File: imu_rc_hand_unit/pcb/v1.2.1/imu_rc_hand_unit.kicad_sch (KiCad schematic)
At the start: 76 parts, among them J1 USB_C_Receptacle_USB2.0_16P, J2 JST SH1.0, Q1 IRLML6344TRPBF, Q2 IRLML6344TRPBF, Q3 DMP3160L-7, Q4 IRLML6344TRPBF, Q5 DMP3160L-7, Q6 BSS138, Q7 BC817-25, Q8 BC817-25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

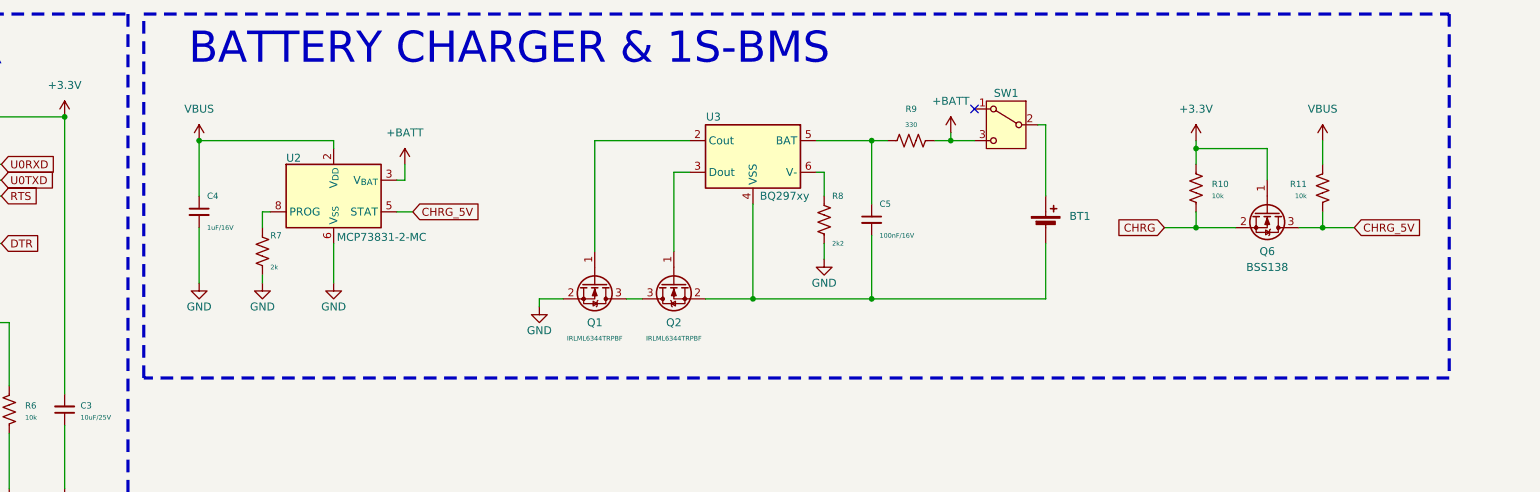
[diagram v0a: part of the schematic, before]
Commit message: commit #39
imu rc hand unit v1.2.2:
removed bq297
added ON/OFF text for switch

enclosure hand unit:
small hole changes inside (m3) and outside (m3)
led diameter hole increased
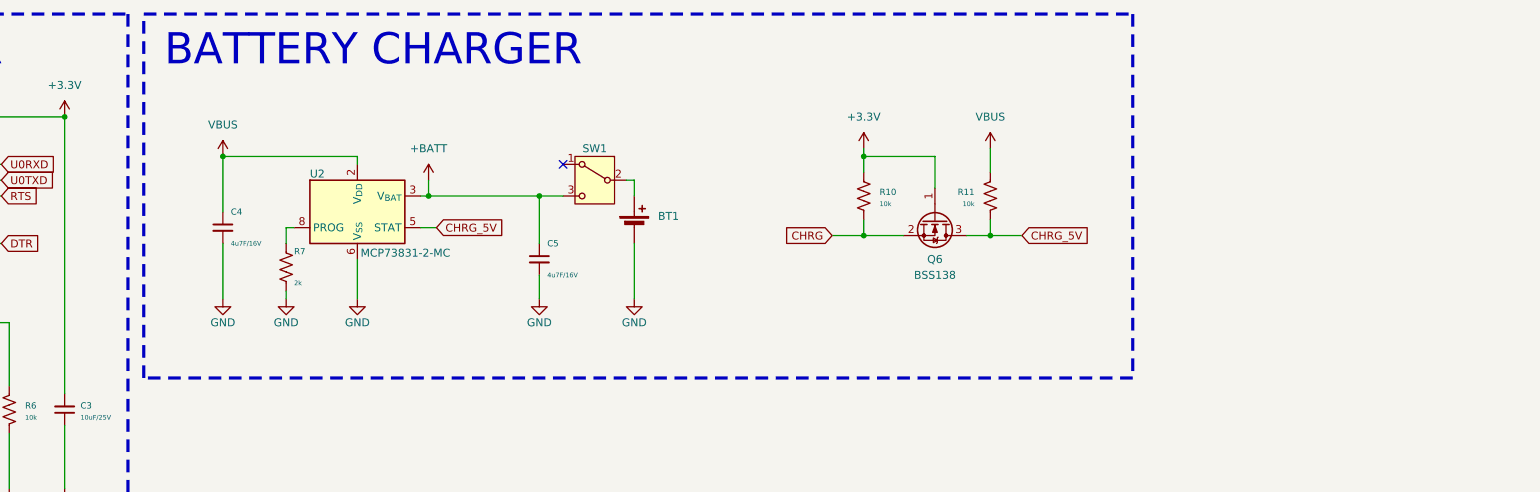
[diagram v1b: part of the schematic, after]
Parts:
- removed Q1, Q2: IRLML6344TRPBF, Package_TO_SOT_SMD:SOT-23, symbol Transistor_FET:AO3400A
- removed R8: 2k2, Resistor_SMD:R_0805_2012Metric, symbol Device:R_US
- removed R9: 330, Resistor_SMD:R_0805_2012Metric, symbol Device:R_US
- removed U3: BQ297xy, Package_SON:WSON-6_1.5x1.5mm_P0.5mm, symbol Battery_Management:BQ297xy
- C4: value 1uF/16V -> 4u7F/16V
- C5: value 100nF/16V -> 4u7F/16V
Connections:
- net +BATT: now also C5.1
- net GND: now also BT1.2 (-), C5.2
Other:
- note added: "BATTERY CHARGER"
- note removed: "BATTERY CHARGER & 1S-BMS"
- title: IMU-RC Hand Unit -> IMU-RC Hand Unit Schematic
- moved on the sheet: BT1, C4, C5, Q6, R10, R11, R7, SW1, U2
